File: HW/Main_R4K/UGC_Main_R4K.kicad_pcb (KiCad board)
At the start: 4 copper layers, 125.7 x 76.4 mm, 160 parts, among them J1 SM02B-SURS-TF_LF__SN_, J10 SM02B-SURS-TF_LF__SN_, J13 503480-0640, J2 503480-0640, J4 Conn_01x06_Pin, J5 UJ31-CH-G1-SMT-TR, J6 Trigger, J7 Trigger, J8 Conn_01x02, J9 Conn_01x02, Q1 MMBT3904, Q2 MMBT3904, Q3 BSS138DW, Q4 BSS138DW, Q5 MMBT2222A, Q6 MMBT2222A, SW1 SW_Push, SW10 SW_Push, SW11 SW_Push, SW12 SW_Push, SW13 SW_Push, SW14 SW_TS-1187A, SW15 1TS026A-1000-0550, SW16 1TS026A-1000-0550, SW17 SW_TS-1187A, SW18 SW_TS-1187A, SW19 SW_TS-1187A, SW2 SW_Push, SW3 SW_Push, SW4 SW_Push, SW5 SW_TS-1187A, SW6 GL18_SW, SW7 SW_Push, SW8 SW_Push, SW9 SW_TS-1187A, U1 ESP32-PICO-MINI-02, U10 ST_LSM6, U11 BQ25180, U12 CH340K, U13 PI3USB4000A, U4 TPS630001RCR, U5 ST_LSM6, U6 MCP3002, U7 MCP3002, U8 RP2040, U9 GD25Q80EEIGR, X1 ModConnect, X2 ModConnect, X3 ModConnect, X4 ModConnect, X5 ModConnect, X6 ModConnect, Y1 Crystal_GND3

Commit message: HW Test branch init
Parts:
- moved J13 1.41 mm to (269.3, 139.8)
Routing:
- net RS_B_IN: track 28.0 -> 26.1 mm
- net RX: track 13.8 -> 15.1 mm
- net +3V3: track 139.1 -> 140.3 mm
- net RS_B_OUT: track 26.4 -> 27.3 mm
- net GND: vias 53 -> 54

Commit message: Update CAD files
- PCB uses a new socket type for the slider potentiometers
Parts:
- added S1: 4015-0-43-80-30-27-10-0, hhl:4015-0-43-80-30-27-10-0, B.Cu at (193.5, 101.4)
- added S2: 4015-0-43-80-30-27-10-0, hhl:4015-0-43-80-30-27-10-0, B.Cu at (191.0, 101.4)
- added S3: 4015-0-43-80-30-27-10-0, hhl:4015-0-43-80-30-27-10-0, B.Cu at (196.0, 101.4)
- added S4: 4015-0-43-80-30-27-10-0, hhl:4015-0-43-80-30-27-10-0, B.Cu at (243.5, 101.4)
- added S5: 4015-0-43-80-30-27-10-0, hhl:4015-0-43-80-30-27-10-0, B.Cu at (241.0, 101.4)
- added S6: 4015-0-43-80-30-27-10-0, hhl:4015-0-43-80-30-27-10-0, B.Cu at (246.0, 101.4)
- RV1, RV2: footprint hhl:GCC_Slider_MillMax -> hhl:GCC_Slider_MillMaxSocketed

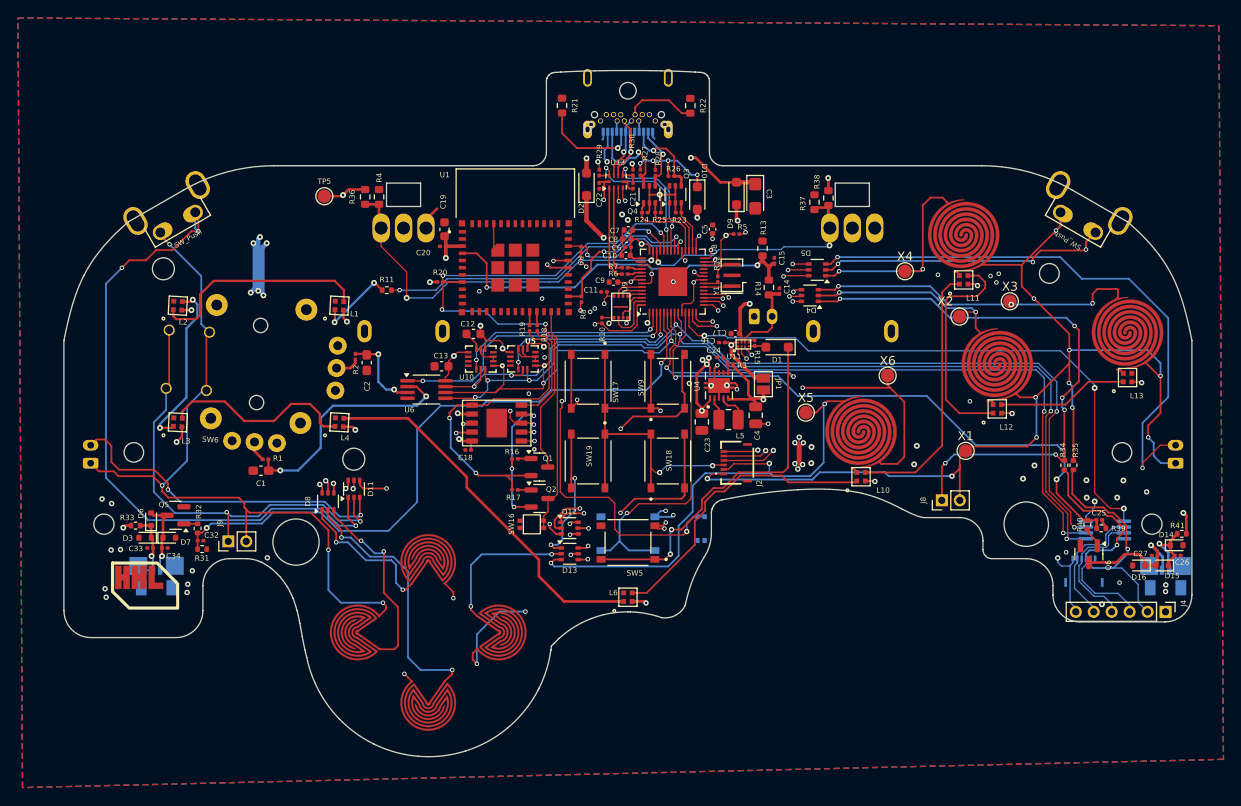
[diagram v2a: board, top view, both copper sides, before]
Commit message: Update PCBs
- New S1 variant
- Update crystal and socket mounts for trigger sliders
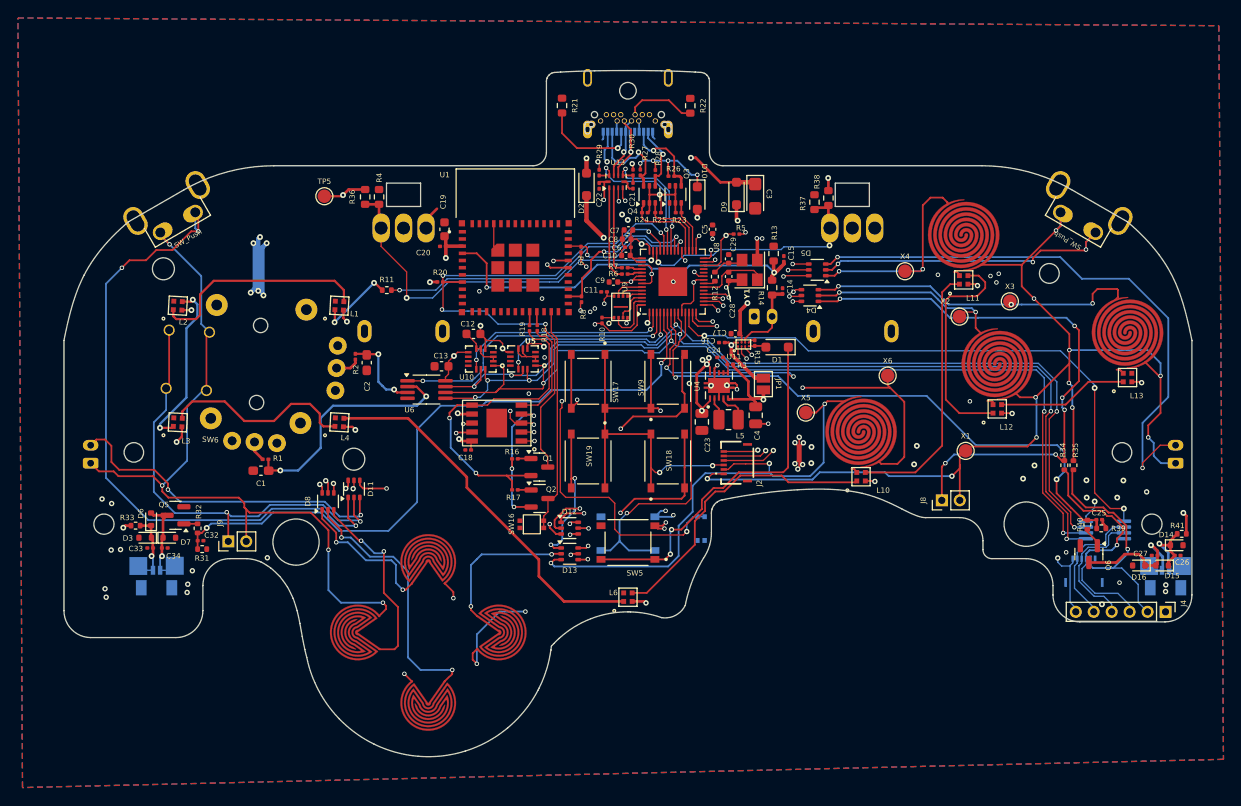
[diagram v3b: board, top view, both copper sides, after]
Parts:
- removed REF**: HHL_Logo, hhl:HHL_Logo
- added C28: 15p, Capacitor_SMD:C_0402_1005Metric, F.Cu at (229.7, 106.8)
- added C29: 15p, Capacitor_SMD:C_0402_1005Metric, F.Cu at (229.7, 104.9)
- R12: footprint Resistor_SMD:R_0201_0603Metric -> Resistor_SMD:R_0402_1005Metric
- Y1: value Crystal_GND3 -> ABM8-272-T3; footprint Crystal:Resonator_SMD_Murata_CSTxExxV-3Pin_3.0x1.1mm -> Crystal:Crystal_SMD_3225-4Pin_3.2x2.5mm
- moved Y1 2.07 mm to (232.1, 106.1)
- moved R13 1.36 mm to (234.7, 104.3)
- moved C15 1.08 mm to (235.9, 104.9)
- moved R12 0.43 mm to (228.2, 106.9), turned to 90 degrees
- moved R14 0.36 mm to (234.5, 108.1)
- moved C14 0.36 mm to (235.7, 108.5)
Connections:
- R12 pad 1: Net-(R12-Pad1) -> XTAL_OUT
- R12 pad 2: XTAL_OUT -> Net-(C29-Pad1)
- Y1 pad 3: Net-(R12-Pad1) -> Net-(C29-Pad1)
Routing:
- net VBUS_SYS: track 40.8 -> 48.5 mm
- net GND: track 50.2 -> 56.4 mm, vias 54 -> 57
- net XTAL_IN: track 3.19 -> 8.11 mm
- net Net-(C29-Pad1): track 0.00 -> 3.58 mm
- net Net-(R12-Pad1): track 2.50 -> 0.00 mm
- net BAT_LVL: track 42.3 -> 44.6 mm
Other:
- board text added: "GCU R4K Designed by Mitch 10.24.2024"
- board text removed: "GCU R4K Designed by Mitch"
